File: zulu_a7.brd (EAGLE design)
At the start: 69.8 x 25.4 mm, 169 parts, among them J1 Pmod 2x6, Q1 12MHz 25ppm (FPGA + FT2232HQ), Q3 MBT3904DW1T1, U1 XC7A35T-1CPG236C, U10 93LC46BT-I/SN, U2 FT2232HQ USB-UART/JTAG Bridge, U3 AS4C32M16SB-6TIN, U4 W25Q128JVSIQ, U8 LTC3569EUDC#TRPBF, X1 Molex 105017-0001 Micro-USB-B

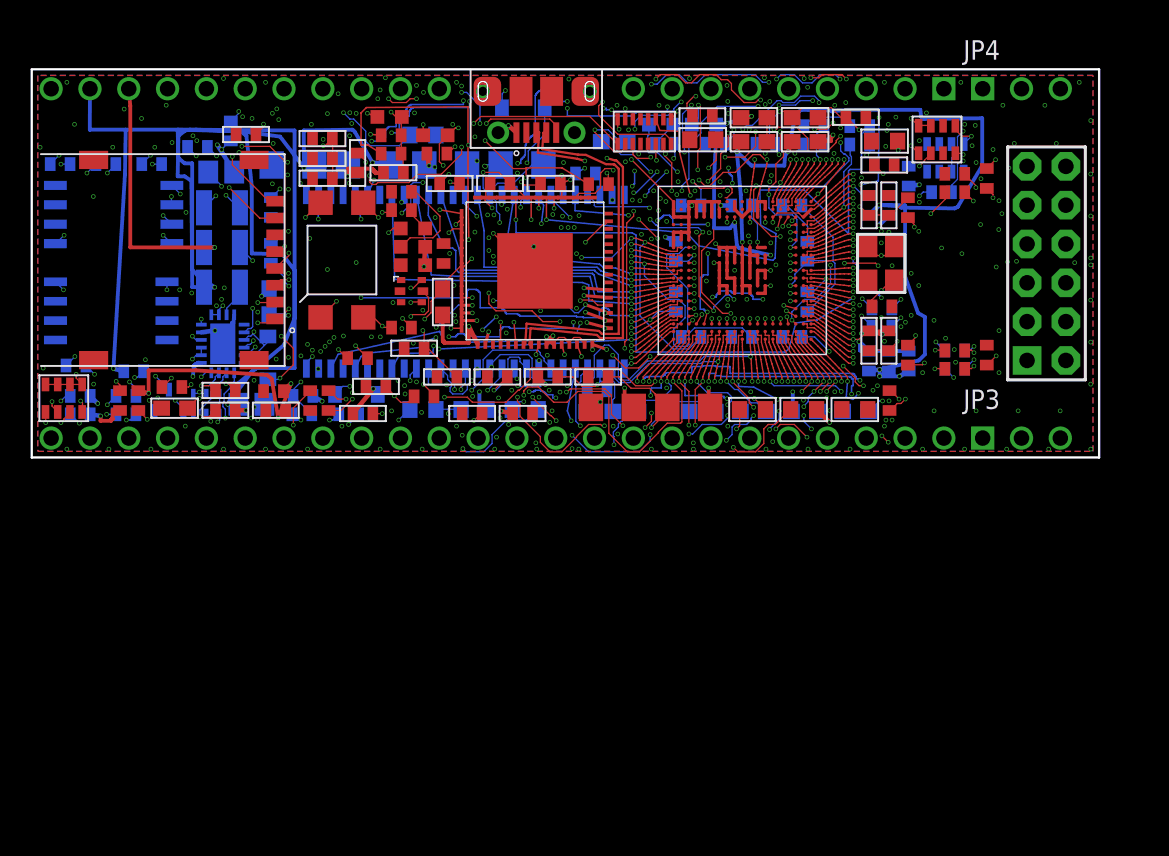
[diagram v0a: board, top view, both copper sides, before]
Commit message: Generate the board: 169 elements, 175 signals, nothing routed
make_board.py and check_board.py both clean. The two share no code, so the
board agreeing with the schematic is two independent readings of the files, not
one function agreeing with itself.

  214 parts -> 169 elements, 45 schematic-only parts correctly have none
  175 signals, 787 contactrefs, 5 pins expanded to several pads
  32 packages across 3 libraries, none missing, none drifted between the files
  238 ball lands at 0.225 mm, 6 copper layers, JLCPCB rules loaded
  0 wires, 0 vias -- unrouted by design

The check that mattered for the last few days of work: "no plated hole of J1,
JP3, JP4, X1, X2 lands on another element, either side." The split JTAG
straddles the Pmod on the real board, not just in the plan.

The schematic came through untouched -- make_board rewrites the 238 ball lands
on its way past and they were already 0.225, so the file is byte-identical.

WHAT IS NOT DONE, AND IT IS THE THING TO LOOK AT FIRST. 144 elements are
placed; 21 are parked below the board. Nine of them are C114-C122, and all nine
are 0.47 uF 0402 -- the high-frequency decoupling, the parts make_board's own
comment calls "the ones that matter" and places before anything else. Four of
those nine are C114, C115, C119 and C120, which is exactly the set the toolchain
recorded JP3 punching through the last time a header stood at x 53.5..60.1.
JP3 and JP4 stand there again, hole_zones() saw them, and the tiler did what it
is supposed to do: it moved the capacitors rather than the header. Moved, here,
means parked.

That is the bill for 2.400 in, and it comes due at routing, not now.

Co-Authored-By: Claude Opus 5 <noreply@anthropic.com>
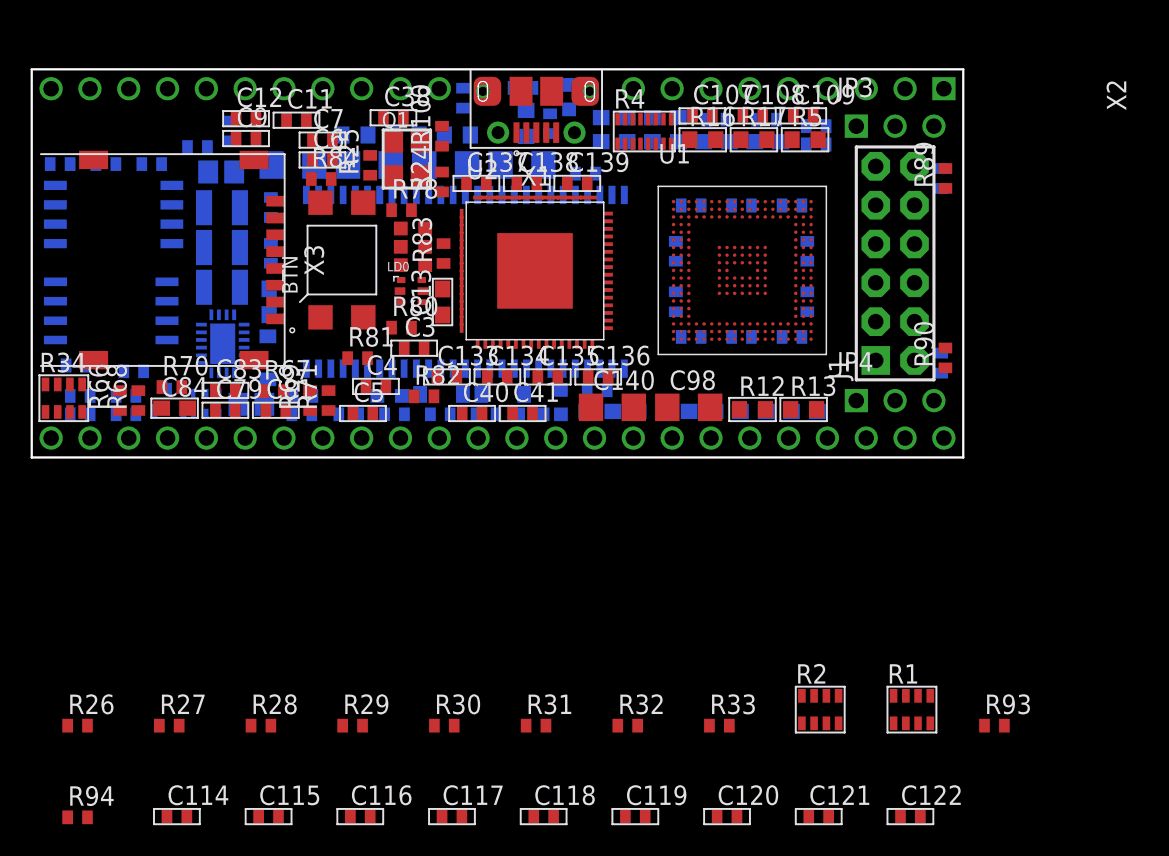
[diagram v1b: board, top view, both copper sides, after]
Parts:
- JP3, JP4: device ctambe:1X03-NOSILK -> pinhead:1X03-NOSILK
- X2: device ctambe:XULA-DIP37 -> ctambe:ZULU-DIP37
- moved R94 68.3 mm to (3.00, -23.6), flipped to the top
- moved R26 62.0 mm to (3.00, -17.6)
- moved R28 57.3 mm to (15.0, -17.6)
- moved R27 57.0 mm to (9.00, -17.6)
- moved R29 53.4 mm to (21.0, -17.6)
- moved C118 50.1 mm to (33.5, -23.5)
- moved C115 48.8 mm to (15.5, -23.5), flipped to the top, turned to 0 degrees
- moved C114 46.9 mm to (9.50, -23.5), flipped to the top, turned to 0 degrees
- moved R31 46.4 mm to (33.0, -17.6), turned to 0 degrees
- moved C119 46.1 mm to (39.5, -23.5)
- moved C122 45.0 mm to (57.5, -23.5), flipped to the top
- moved C121 44.5 mm to (51.5, -23.5), flipped to the top
- moved C120 44.2 mm to (45.5, -23.5), flipped to the top
- moved C117 43.7 mm to (27.5, -23.5), flipped to the top, turned to 0 degrees
- moved R30 43.0 mm to (27.0, -17.6), turned to 0 degrees
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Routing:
- net VCC3V3: track 443.0 -> 0.00 mm, vias 84 -> 0
- net GND: track 245.7 -> 0.00 mm, vias 180 -> 0
- net VCC1V0: track 231.7 -> 0.00 mm, vias 15 -> 0
- net TMS: track 123.6 -> 0.00 mm, vias 18 -> 0
- net TDI: track 122.4 -> 0.00 mm, vias 19 -> 0
- net VCC1V8: track 121.9 -> 0.00 mm, vias 12 -> 0
- net TCK: track 116.7 -> 0.00 mm, vias 17 -> 0
- net D3: track 115.3 -> 0.00 mm, vias 9 -> 0
- net UART_FT_RTS#: track 98.0 -> 0.00 mm, vias 2 -> 0
- net FLASH-CS#: track 95.0 -> 0.00 mm, vias 14 -> 0
- net BS0: track 93.8 -> 0.00 mm, vias 10 -> 0
- net SD-CMD: track 90.5 -> 0.00 mm, vias 13 -> 0
- net AIN15_P: track 89.8 -> 0.00 mm, vias 10 -> 0
- net VU: track 78.7 -> 0.00 mm, vias 11 -> 0
- net FPGA-TMS: track 78.5 -> 0.00 mm, vias 8 -> 0
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- removed copper zone on layer 1, net GND
- removed copper zone on layer 16, net GND
- removed copper zone on layer 2, net GND
- removed copper zone on layer 5, net VCC3V3
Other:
- board size 69.8 x 25.4 mm -> 61 x 25.4 mm

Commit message: All 39 FPGA decoupling capacitors placed; the fields follow the ring now
The nine parked 0.47 uF were a symptom. tile() was placing ZERO of the 35
capacitors it is handed -- not nine short, none at all -- and the anchored pass
further down was quietly catching 25 of them. The decoupling was not nearly
right with a few gaps. It was unplanned, and it looked nearly right.

WHY. The four fields were fixed boxes hugging the package, sized when Q1 sat at
x 53.79 and capped the escape's fan-out ring at 6.94 half-width. Moving Q1 off
the +x end for the split JTAG, and then again out from between the USB and the
FT2232, left nothing capping the ring, so it opened to its full 7.64 -- exactly
the figure make_board's own comment says Q1 permitted at x 54.04. The ring is
now (38.86..54.14) x (4.60..19.88), and all four fields were inside it. BELOW
sat wholly within one ring box while measuring 100 % free, which is what took
so long to see: the space was empty, and reserved.

The ring growing is the good outcome -- 6 stage-3 conflicts at 7.40 against 11
at 6.94 -- so the ring is the given and the fields move. They are derived from
RING now instead of restating numbers beside it, so the next time it moves they
follow rather than going quietly stale.

ORDER MATTERS MORE THAN AREA. Widening the strips to the length of the board
placed all 39 and put 0.47 uF capacitors 27 mm from the ball field, because
tile() fills from x0 and a wide strip hands its first parts the far end. That is
not decoupling, it is a capacitor that fits. So the ring's own width is offered
first and the long strips only pick up the overflow:

  0.47 uF  22 placed, 8.4 to 9.7 mm from the ball centre, median 9.3
  4.7 uF   11 placed, median 22.3
  47 uF     6 placed, median 24.4 -- bulk belongs at the regulator anyway

LEFT is deleted. At 7.64 half-width it is inside the ring on one side and under
U3 on the back on the other; there is no lane there any more.

Parked drops 25 -> 14, of which 4 are the padless CC ar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
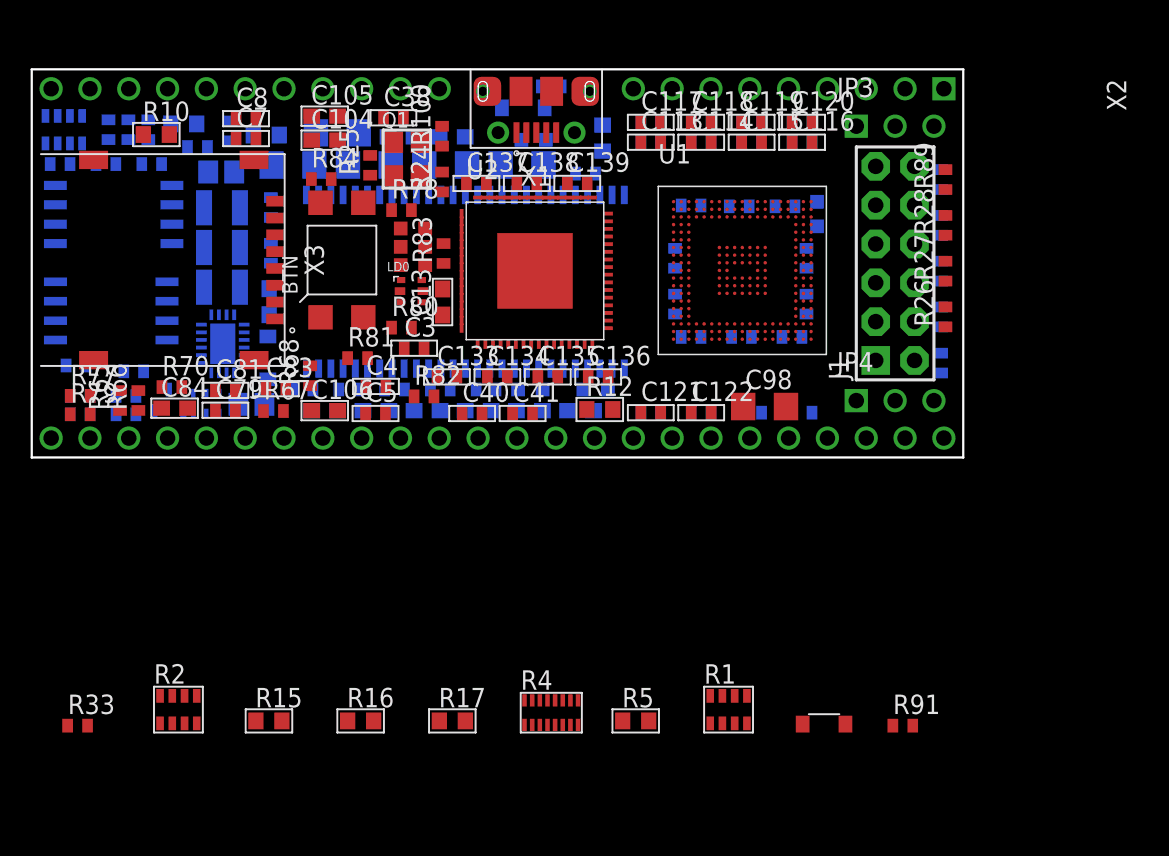
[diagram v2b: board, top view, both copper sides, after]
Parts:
- moved R26 62.8 mm to (59.8, 9.20), turned to 90 degrees
- moved R94 60.1 mm to (50.7, 13.0), flipped to the bottom, turned to 90 degrees
- moved R27 58.9 mm to (59.8, 12.2), turned to 90 degrees
- moved C114 55.9 mm to (43.8, 20.6)
- moved R28 55.5 mm to (59.8, 15.2), turned to 90 degrees
- moved C115 54.3 mm to (47.1, 20.6)
- moved C116 52.8 mm to (50.4, 20.6)
- moved C117 47.3 mm to (40.5, 21.9)
- moved R29 46.9 mm to (59.5, 9.20), flipped to the bottom, turned to 90 degrees
- moved C118 46.6 mm to (43.8, 21.9)
- moved C119 46.1 mm to (47.1, 21.9)
- moved C120 45.7 mm to (50.4, 21.9)
- moved R16 44.1 mm to (21.5, -17.2)
- moved R30 44.1 mm to (59.5, 12.2), flipped to the bottom, turned to 90 degrees
- moved R17 42.8 mm to (27.5, -17.2)
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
